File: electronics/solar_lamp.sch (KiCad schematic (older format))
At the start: 27 parts, among them U1 ATmega32U4-AU, X1 CRYSTAL

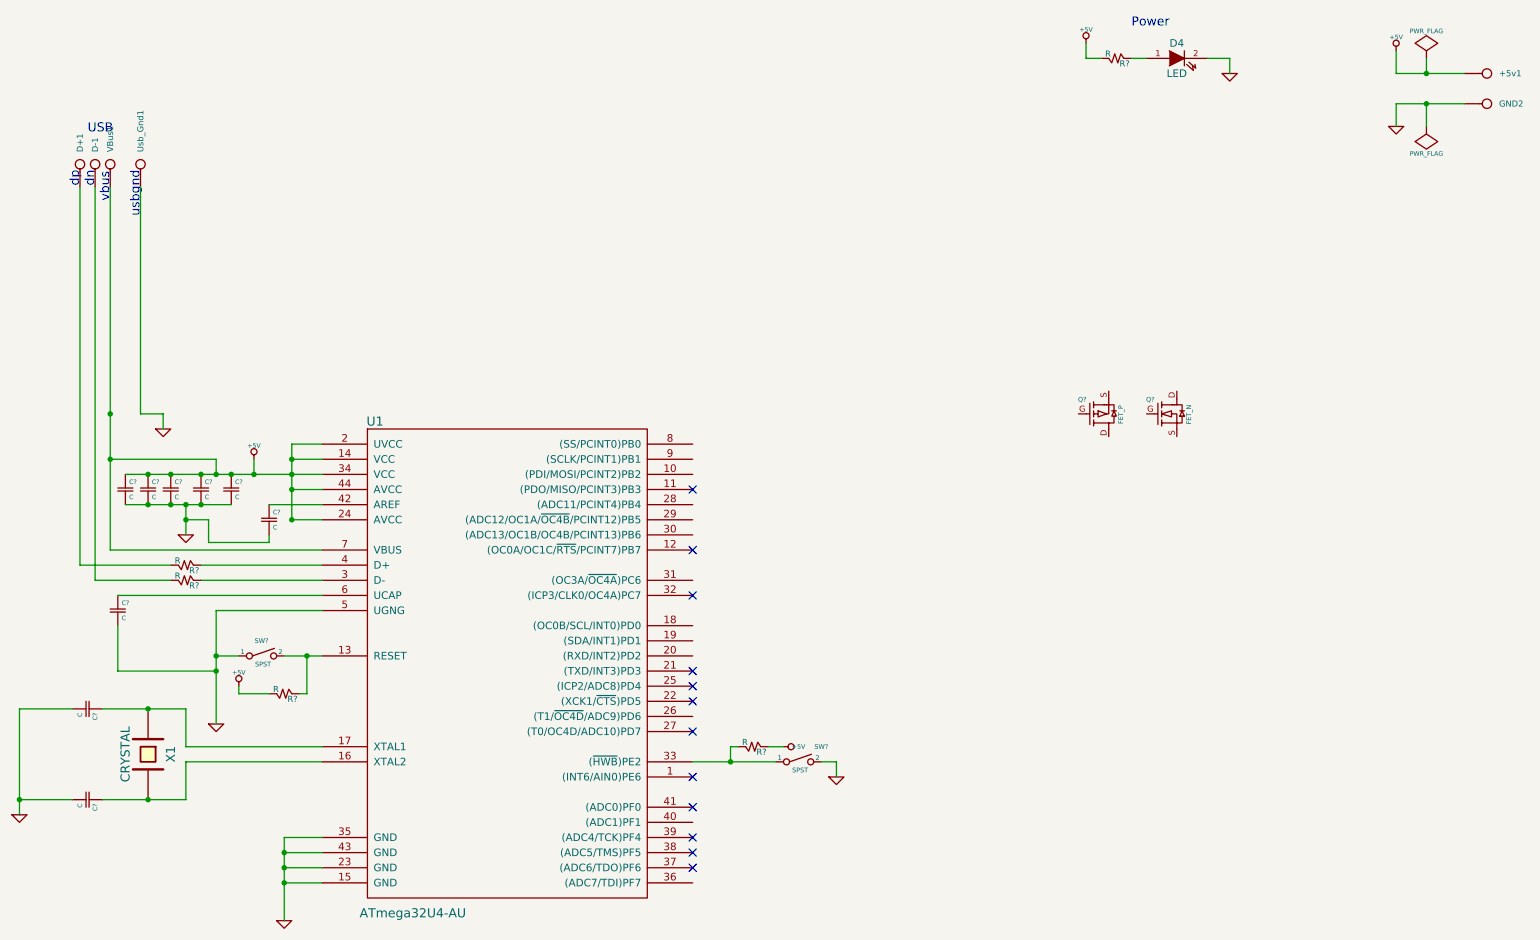
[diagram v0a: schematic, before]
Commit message: created smaller components in schematic, started layout with ideal diodes and synchronous rectification
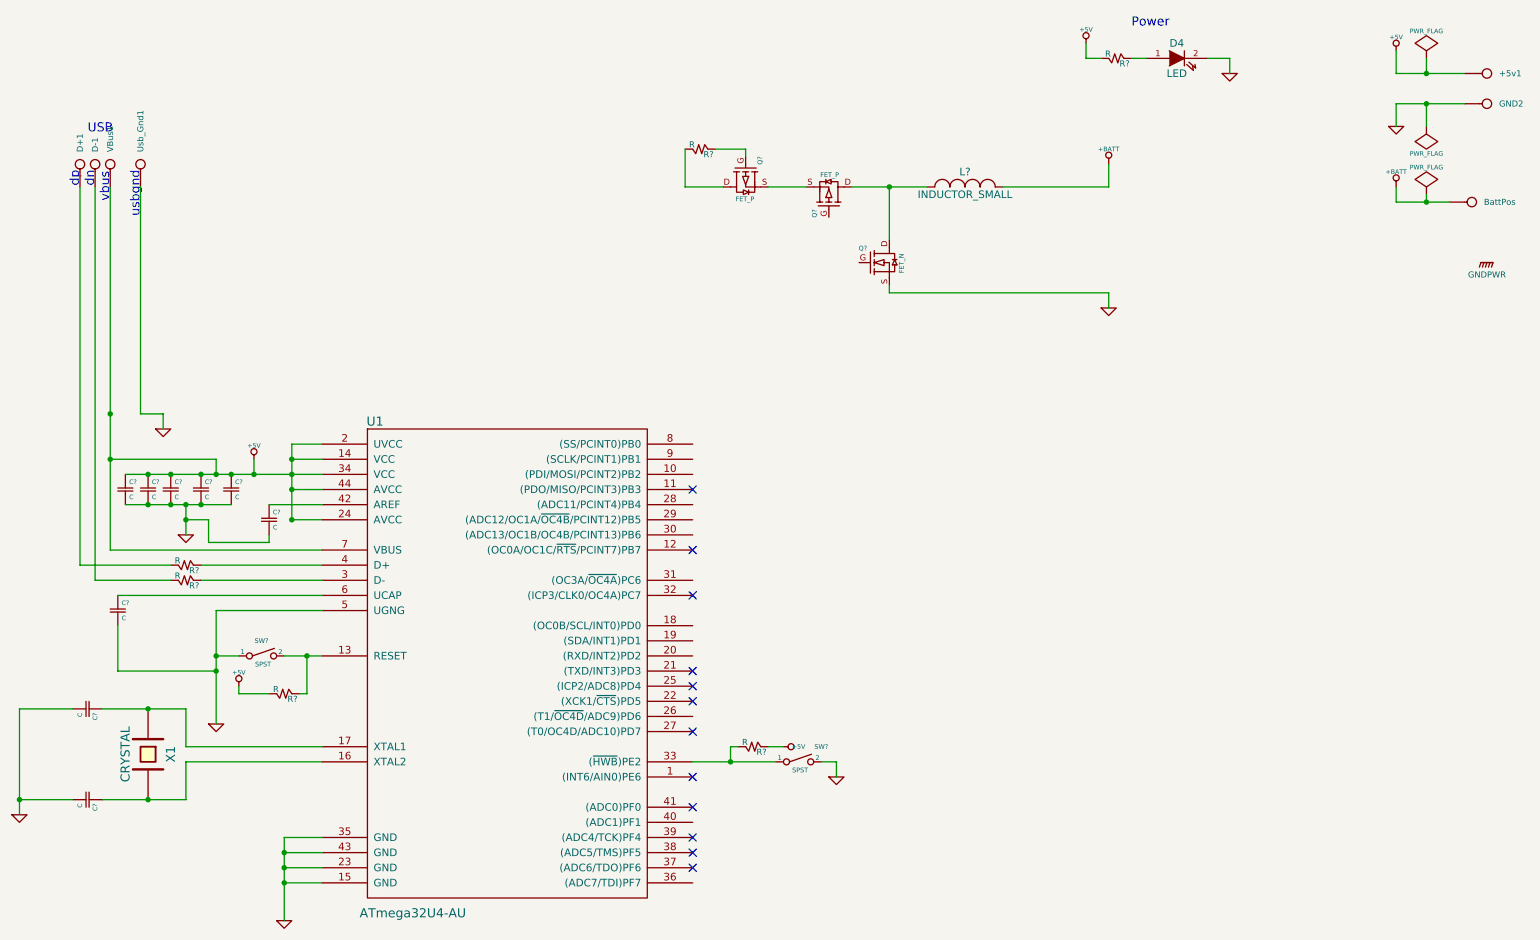
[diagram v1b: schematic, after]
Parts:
- added BattPos: CONN_1, symbol CONN_1
- added L?: INDUCTOR_SMALL, symbol INDUCTOR_SMALL
- added Q?: FET_P, symbol FET_P
- added R?: R, symbol R
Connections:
- net GND: now also Q?.S
- net at Q?.D: now also Q?.D, L?.1
- net at Q?.S: now also Q?.S
- new net: Q?.D, R?.2
- new net: Q?.G, R?.1
- new net +BATT: BattPos.1, L?.2
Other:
- moved on the sheet: Q?
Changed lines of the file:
@@
 	2500 4150 2500 4100
 Wire Wire Line
-	2400 3600 2400 3700
+	2400 3700 2400 3600
 Connection ~ 2400 3700
 Wire Wire Line
@@
 	6250 5600 6150 5600
 Wire Wire Line
-	5850 5600 5300 5600
+	5300 5600 5850 5600
 Wire Wire Line
 	5900 5500 5800 5500
@@
 L FET_P Q?
 U 1 1 53C4149E
-P 7950 3300
-F 0 "Q?" H 7875 3395 31  0000 C CNN
-F 1 "FET_P" V 8130 3295 31  0000 C CNN
-F 2 "" H 7950 3300 60  0000 C CNN
-F 3 "" H 7950 3300 60  0000 C CNN
-	1    7950 3300
-	1    0    0    -1
+P 6200 1900
+F 0 "Q?" H 6125 1995 31  0000 C CNN
+F 1 "FET_P" V 6380 1895 31  0000 C CNN
+F 2 "" H 6200 1900 60  0000 C CNN
+F 3 "" H 6200 1900 60  0000 C CNN
+	1    6200 1900
+	0    -1   -1   0
 $EndComp
 $Comp
 L FET_N Q?
 U 1 1 53C419AE
-P 8400 3300
-F 0 "Q?" H 8325 3395 31  0000 C CNN
-F 1 "FET_N" V 8580 3295 31  0000 C CNN
-F 2 "" H 8400 3300 60  0000 C CNN
-F 3 "" H 8400 3300 60  0000 C CNN
-	1    8400 3300
-	1    0    0    -1
-$EndComp
+P 6500 2300
+F 0 "Q?" H 6425 2395 31  0000 C CNN
+F 1 "FET_N" V 6680 2295 31  0000 C CNN
+F 2 "" H 6500 2300 60  0000 C CNN
+F 3 "" H 6500 2300 60  0000 C CNN
+	1    6500 2300
+	1    0    0    -1
+$EndComp
+$Comp
+L FET_P Q?
+U 1 1 53CA56C5
+P 5650 1700
+F 0 "Q?" H 5575 1795 31  0000 C CNN
+F 1 "FET_P" V 5830 1695 31  0000 C CNN
+F 2 "" H 5650 1700 60  0000 C CNN
+F 3 "" H 5650 1700 60  0000 C CNN
+	1    5650 1700
+	0    1    1    0
+$EndComp
+$Comp
+L INDUCTOR_SMALL L?
+U 1 1 53CA956A
+P 7100 1800
+F 0 "L?" H 7100 1900 50  0000 C CNN
+F 1 "INDUCTOR_SMALL" H 7100 1750 50  0000 C CNN
+F 2 "" H 7100 1800 60  0000 C CNN
+F 3 "" H 7100 1800 60  0000 C CNN
+	1    7100 1800
+	1    0    0    -1
+$EndComp
+$Comp
+L CONN_1 BattPos
+U 1 1 53CA9786
+P 10450 1900
+F 0 "BattPos" H 10530 1900 40  0000 L CNN
+F 1 "CONN_1" H 10450 1955 30  0001 C CNN
+F 2 "" H 10450 1900 60  0000 C CNN
+F 3 "" H 10450 1900 60  0000 C CNN
+	1    10450 1900
+	1    0    0    -1
+$EndComp
+$Comp
+L +BATT #PWR?
+U 1 1 53CA9989
+P 9950 1800
+F 0 "#PWR?" H 9950 1750 20  0001 C CNN
+F 1 "+BATT" H 9950 1900 30  0000 C CNN
+F 2 "" H 9950 1800 60  0000 C CNN
+F 3 "" H 9950 1800 60  0000 C CNN
+	1    9950 1800
+	1    0    0    -1
+$EndComp
+$Comp
+L PWR_FLAG #FLG?
+U 1 1 53CA99B9
+P 10150 1850
+F 0 "#FLG?" H 10150 1945 30  0001 C CNN
+F 1 "PWR_FLAG" H 10150 2030 30  0000 C CNN
+F 2 "" H 10150 1850 60  0000 C CNN
+F 3 "" H 10150 1850 60  0000 C CNN
+	1    10150 1850
+	1    0    0    -1
+$EndComp
+Wire Wire Line
+	9950 1900 10300 1900
+Wire Wire Line
+	9950 1900 9950 1800
+Wire Wire Line
+	10150 1900 10150 1850
+Connection ~ 10150 1900
+$Comp
+L +BATT #PWR?
+U 1 1 53CA9BE8
+P 8050 1650
+F 0 "#PWR?" H 8050 1600 20  0001 C CNN
+F 1 "+BATT" H 8050 1750 30  0000 C CNN
+F 2 "" H 8050 1650 60  0000 C CNN
+F 3 "" H 8050 1650 60  0000 C CNN
+	1    8050 1650
+	1    0    0    -1
+$EndComp
+$Comp
+L R R?
+U 1 1 53CA9DD8
+P 5350 1550
+F 0 "R?" V 5385 1605 40  0000 C CNN
+F 1 "R" V 5320 1495 40  0000 C CNN
+F 2 "" V 5280 1550 30  0000 C CNN
+F 3 "" H 5350 1550 30  0000 C CNN
+	1    5350 1550
+	0    1    1    0
+$EndComp
+Wire Wire Line
+	5650 1600 5650 1550
+Wire Wire Line
+	5650 1550 5450 1550
+Wire Wire Line
+	5250 1550 5250 1800
+Wire Wire Line
+	5250 1800 5500 1800
+Wire Wire Line
+	5800 1800 6050 1800
+Wire Wire Line
+	6350 1800 6850 1800
+Wire Wire Line
+	6600 2150 6600 1800
+Connection ~ 6600 1800
+Wire Wire Line
+	7350 1800 8050 1800
+Wire Wire Line
+	8050 1800 8050 1650
+Wire Wire Line
+	6600 2450 6600 2500
+Wire Wire Line
+	6600 2500 8050 2500
+$Comp
+L GND #PWR?
+U 1 1 53CAB132
+P 8050 2600
+F 0 "#PWR?" H 8050 2600 30  0001 C CNN
+F 1 "GND" H 8050 2530 30  0001 C CNN
+F 2 "" H 8050 2600 60  0000 C CNN
+F 3 "" H 8050 2600 60  0000 C CNN
+	1    8050 2600
+	1    0    0    -1
+$EndComp
+Wire Wire Line
+	8050 2500 8050 2600
+$Comp
+L GNDPWR #PWR?
+U 1 1 53CAB5EB
+P 10550 2300
+F 0 "#PWR?" H 10550 2350 40  0001 C CNN
+F 1 "GNDPWR" H 10550 2220 40  0000 C CNN
+F 2 "" H 10550 2300 60  0000 C CNN
+F 3 "" H 10550 2300 60  0000 C CNN
+	1    10550 2300
+	1    0    0    -1
+$EndComp
